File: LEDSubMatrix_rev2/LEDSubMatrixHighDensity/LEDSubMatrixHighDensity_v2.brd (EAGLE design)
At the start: 16.9 x 146 mm, 145 parts, among them IC1 TLC5955DCAR, IC2 TLC5955DCAR, IC3 TLC5955DCAR, IC4 TLC5955DCAR, IC5 TLC5955DCAR, IC6 TLC5955DCAR, IC7 TLC5955DCAR, IC8 TLC5955DCAR

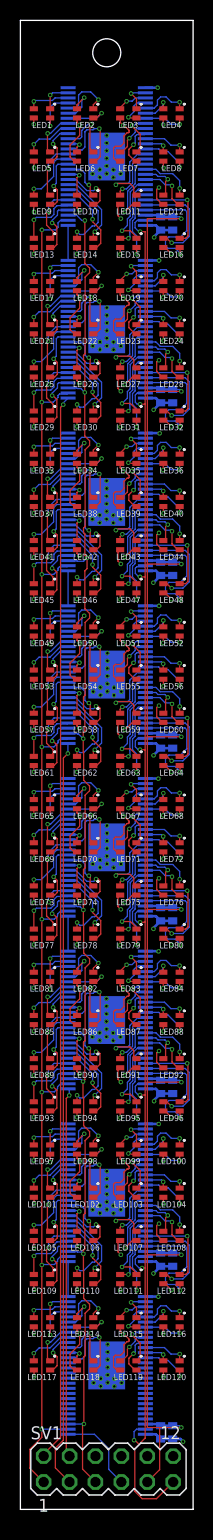
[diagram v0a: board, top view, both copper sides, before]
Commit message: Updated pinouts to align with control board
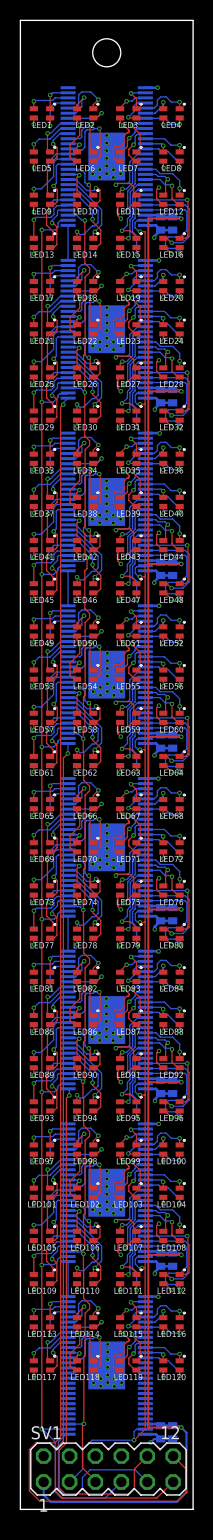
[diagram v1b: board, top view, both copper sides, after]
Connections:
- net 3V3_LOGIC: now also SV1.1; no longer SV1.9
- net GND: now also SV1.2, SV1.4; no longer SV1.10, SV1.12
- net GSCLK: now also SV1.3; no longer SV1.11
- net SCLK: now also SV1.7; no longer SV1.1
- net SIN_1,2: now also SV1.12; no longer SV1.2
- net SIN_3,4: now also SV1.11; no longer SV1.3
- net SIN_5,6: now also SV1.10; no longer SV1.4
- net SIN_7,8: now also SV1.9; no longer SV1.7
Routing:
- net SIN_1,2: track 104.7 -> 130.0 mm
- net 3V3_LOGIC: track 180.4 -> 196.3 mm
- net SIN_5,6: track 36.3 -> 51.2 mm
- net SIN_3,4: track 73.5 -> 86.3 mm
- net SIN_7,8: track 8.36 -> 17.0 mm
- net SCLK: track 147.8 -> 155.8 mm
- net GSCLK: track 150.7 -> 149.5 mm
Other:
- board text added: "Voxel LED Submatrix rev 2"
